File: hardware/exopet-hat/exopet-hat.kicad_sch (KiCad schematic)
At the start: 44 parts, among them J1 12V DC in, J10 CH3 12V OUT, J11 CH4 dry contact, J2 12V screw term, J3 RPi GPIO (HAT), J4 DS18B20 TRS jack, J5 DS18B20 JST, J8 CH1 12V OUT, J9 CH2 12V OUT, K1 G5LE-1 DC12, K2 G5LE-1 DC12, K3 G5LE-1 DC12, K4 G5LE-1 DC12, Q1 DMP4015SK3, U2 TBD62003APG, U4 CAT24C32, U5 TPD1E10B06

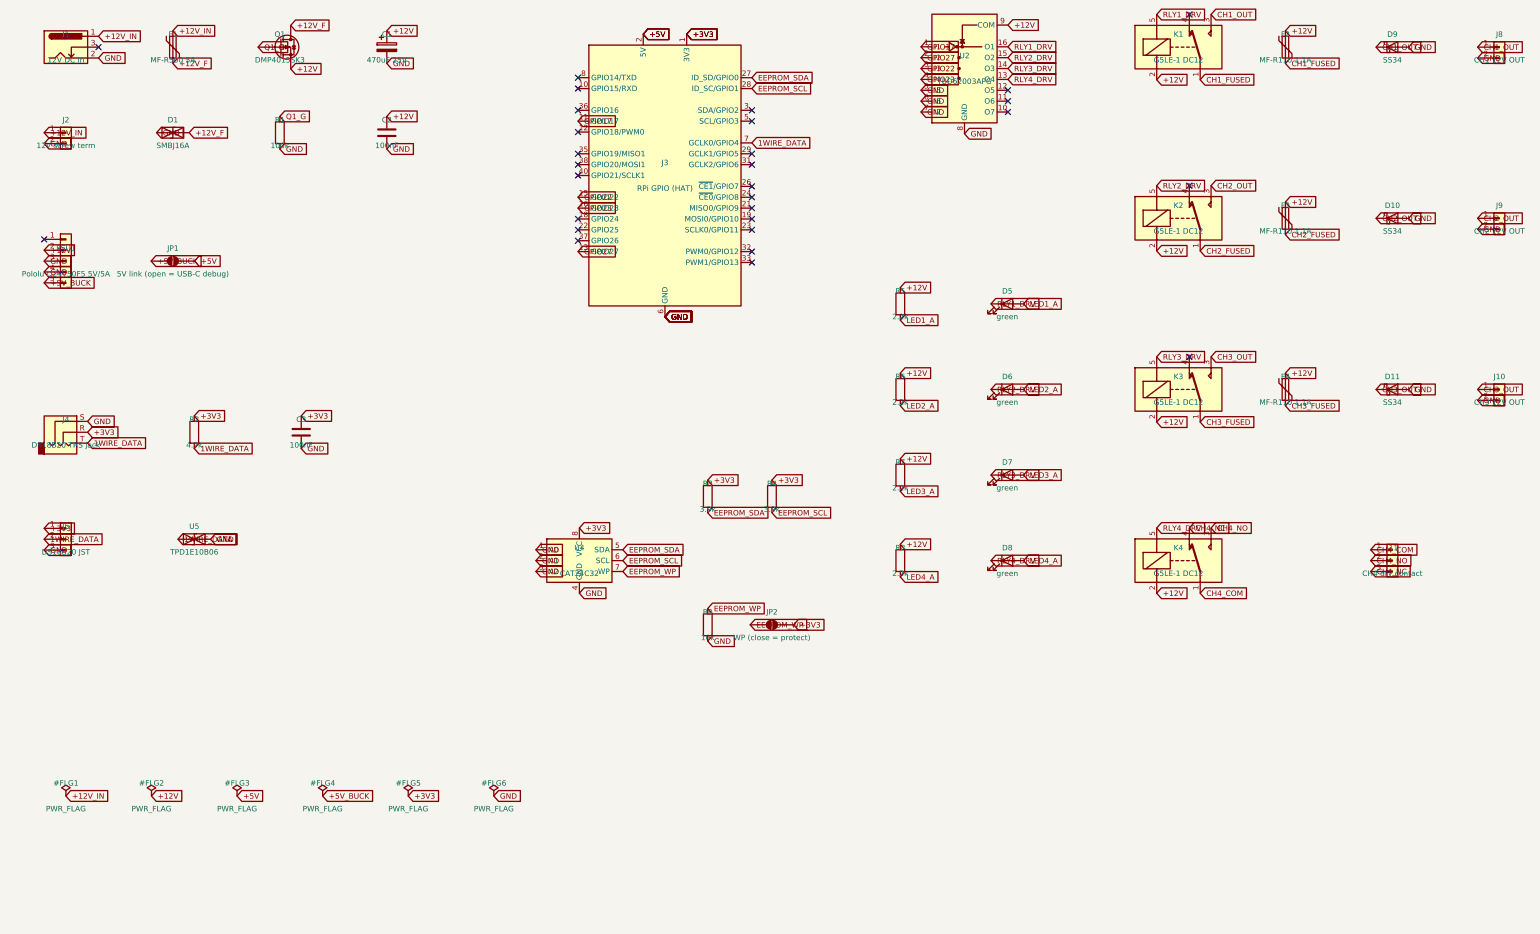
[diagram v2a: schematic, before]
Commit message: Assign footprints and LCSC part numbers to HAT schematic (stage 2)
- Every component has a footprint from the official KiCad libs (all
  verified to exist locally); BOM CSV exported grouped by value
- Web-verified LCSC picks: G5LE-1-CF relay C1524650, TBD62003AFG
  driver C163227 (SOIC), AOD403 P-FET C28969 (replaces unstocked
  DMP4015SK3)
- Added missing C4 EEPROM decoupling cap from spec
- BOM-NOTES.md records confidence per part and order-time checklist
- ERC still 0/0; netlist sanity re-verified

Co-Authored-By: Claude Fable 5 <noreply@anthropic.com>
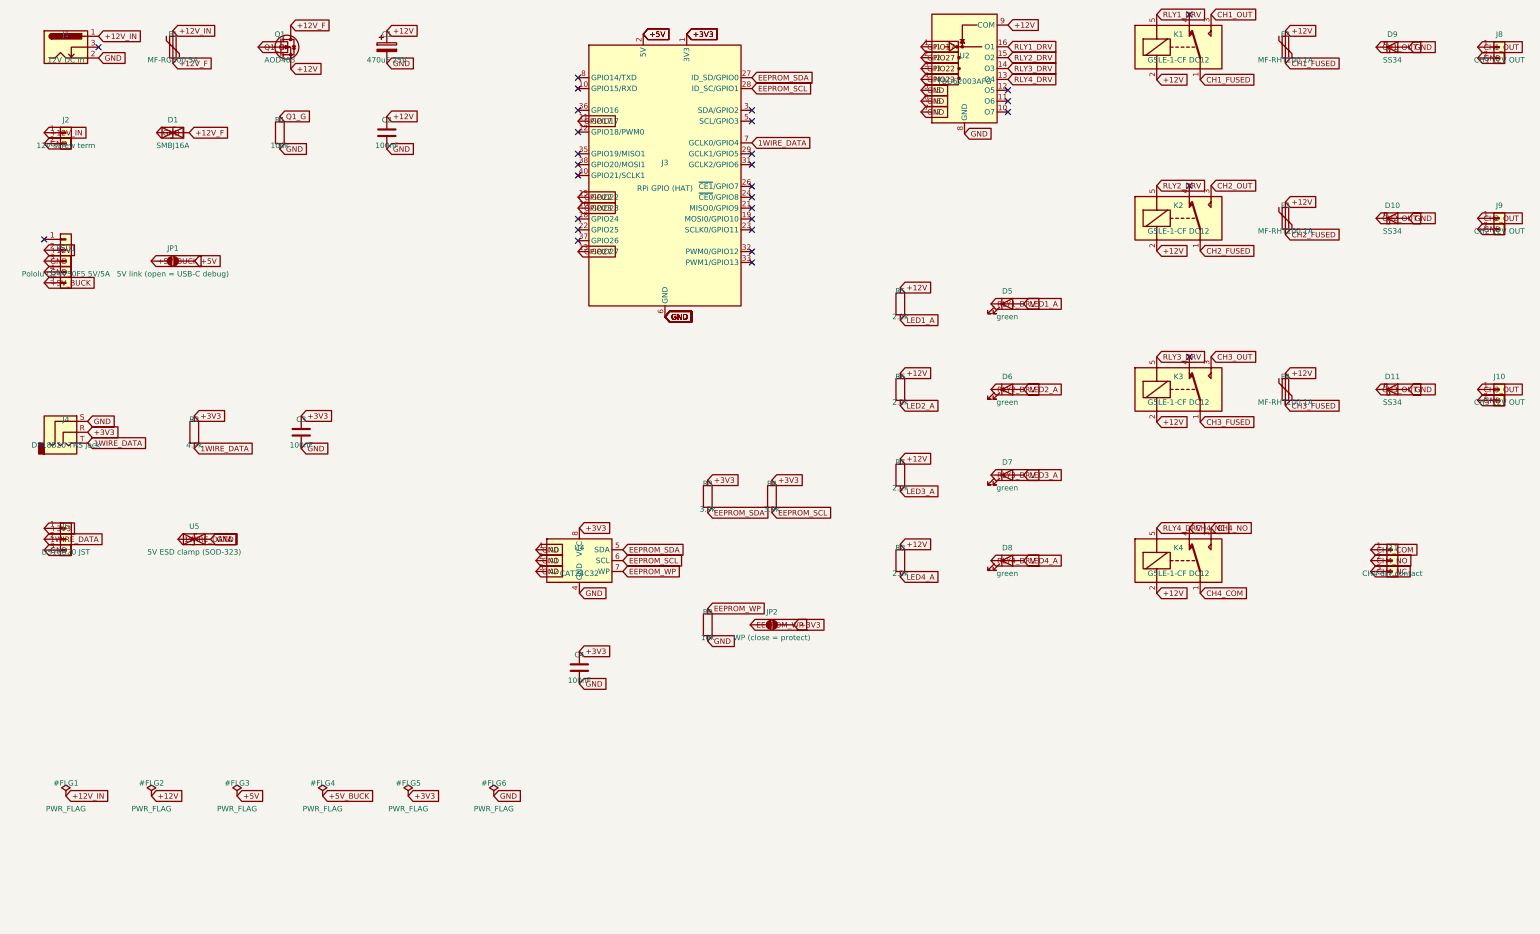
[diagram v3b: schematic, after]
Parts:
- added C4: 100nF, Capacitor_SMD:C_0805_2012Metric, symbol Device:C
- C1: footprint (none) -> Capacitor_THT:CP_Radial_D8.0mm_P3.50mm; LCSC (none) -> VERIFY
- C2, C3: footprint (none) -> Capacitor_SMD:C_0805_2012Metric; LCSC (none) -> C49678
- D1: footprint (none) -> Diode_SMD:D_SMB; LCSC (none) -> VERIFY
- D10, D11, D9: footprint (none) -> Diode_SMD:D_SMA; LCSC (none) -> C8678
- D5, D6, D7, D8: footprint (none) -> LED_SMD:LED_0805_2012Metric; LCSC (none) -> C2297
- F1: value MF-R500 5A -> MF-RG500 5A; footprint (none) -> Fuse:Fuse_Bourns_MF-RG500; LCSC (none) -> VERIFY
- F2, F3, F4: value MF-R110 1.1A -> MF-RHT100 1A; footprint (none) -> Fuse:Fuse_Bourns_MF-RHT100; LCSC (none) -> VERIFY
- J10, J2, J8, J9: footprint TerminalBlock:TerminalBlock_bornier-2_P5.08mm -> TerminalBlock_Phoenix:TerminalBlock_Phoenix_MKDS-1,5-2-5.08_1x02_P5.08mm_Horizontal
- J11: footprint TerminalBlock:TerminalBlock_bornier-3_P5.08mm -> TerminalBlock_Phoenix:TerminalBlock_Phoenix_MKDS-1,5-3-5.08_1x03_P5.08mm_Horizontal
- J3: footprint (none) -> Connector_PinSocket_2.54mm:PinSocket_2x20_P2.54mm_Vertical
- J4: footprint (none) -> Connector_Audio:Jack_3.5mm_CUI_SJ-3523-SMT_Horizontal
- J5: footprint (none) -> Connector_JST:JST_XH_B3B-XH-A_1x03_P2.50mm_Vertical
- JP1, JP2: footprint (none) -> Jumper:SolderJumper-2_P1.3mm_Open_RoundedPad1.0x1.5mm
- K1, K2, K3, K4: value G5LE-1 DC12 -> G5LE-1-CF DC12; LCSC (none) -> C1524650
- PSU1: footprint (none) -> Connector_PinSocket_2.54mm:PinSocket_1x05_P2.54mm_Vertical
- Q1: value DMP4015SK3 -> AOD403; footprint (none) -> Package_TO_SOT_SMD:TO-252-2; LCSC (none) -> C28969
- R1: footprint (none) -> Resistor_SMD:R_0805_2012Metric; LCSC (none) -> C17407
- R2: footprint (none) -> Resistor_SMD:R_0805_2012Metric; LCSC (none) -> C17673
- R3, R4: footprint (none) -> Resistor_SMD:R_0805_2012Metric; LCSC (none) -> C26010
- R5, R6, R7, R8: footprint (none) -> Resistor_SMD:R_0805_2012Metric; LCSC (none) -> C17520
- R9: footprint (none) -> Resistor_SMD:R_0805_2012Metric; LCSC (none) -> C17414
- U2: value TBD62003APG -> TBD62003AFG; footprint (none) -> Package_SO:SOIC-16_3.9x9.9mm_P1.27mm; LCSC (none) -> C163227
- U4: footprint (none) -> Package_SO:SOIC-8_3.9x4.9mm_P1.27mm; LCSC (none) -> VERIFY
- U5: value TPD1E10B06 -> 5V ESD clamp (SOD-323); footprint (none) -> Diode_SMD:D_SOD-323; LCSC (none) -> VERIFY
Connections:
- net +3V3: now also C4.1
- net GND: now also C4.2

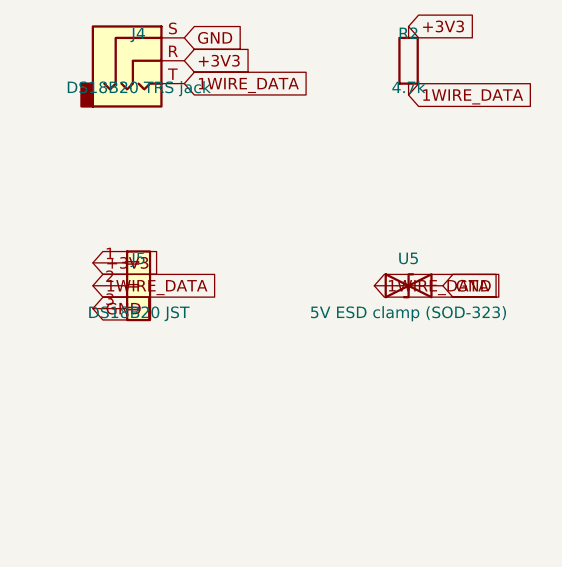
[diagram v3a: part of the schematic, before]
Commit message: Route ExoPet HAT board: generated placement + autoroute, DRC clean
- tools/gen_board.py builds the .kicad_pcb from the schematic netlist
  (footprints, per-pad nets, engineered placement, HAT outline/holes)
- All SMD on the back side in pin-free channels; top side THT only
- freerouting autoroutes (100 connections, 0 unrouted); GND pours both
  sides added and filled via pcbnew scripting
- DRC: 0 errors except 3 documented courtyard overlaps from
  flush-ganged terminal blocks
- Layout-driven design deltas: J5 JST temp connector cut (TRS only),
  J2 12V screw input became solder wire pads; schematic + BOM updated
- 3D renders of both sides included

Co-Authored-By: Claude Fable 5 <noreply@anthropic.com>
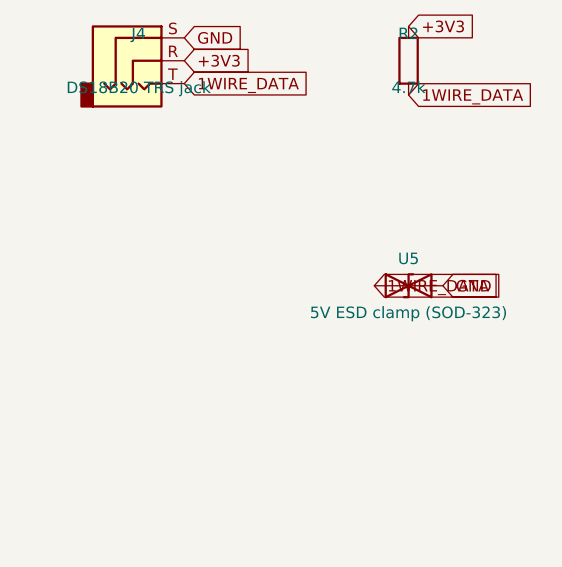
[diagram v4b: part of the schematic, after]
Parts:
- removed J5: DS18B20 JST, Connector_JST:JST_XH_B3B-XH-A_1x03_P2.50mm_Vertical, symbol Connector_Generic:Conn_01x03
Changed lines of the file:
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@@
-    )
-  )
-  (symbol (lib_id "Connector_Generic:Conn_01x03") (at 30 155 0) (unit 1)
-    (exclude_from_sim no) (in_bom yes) (on_board yes) (dnp no)
-    (property "Reference" "J5" (at 30 152 0) (effects (font (size 1.27 1.27))))
-    (property "Value" "DS18B20 JST" (at 30 158 0) (effects (font (size 1.27 1.27))))
-    (property "Footprint" "Connector_JST:JST_XH_B3B-XH-A_1x03_P2.50mm_Vertical" (at 30 155 0) (effects (font (size 1.27 1.27)) hide))
-    (property "LCSC" "" (at 30 155 0) (effects (font (size 1.27 1.27)) hide))
-    (pin "1")
-    (pin "2")
-    (pin "3")
-    (instances
-      (project "exopet-hat"
-        (path "/e0a7e100-0000-4000-8000-00000000c0de" (reference "J5") (unit 1))
-      )
     )
   )
@@
   (global_label "+3V3" (shape input) (at 35.08 130.0 0) (effects (font (size 1.27 1.27)) (justify left)))
   (global_label "1WIRE_DATA" (shape input) (at 35.08 132.54 0) (effects (font (size 1.27 1.27)) (justify left)))
-  (global_label "+3V3" (shape input) (at 24.92 152.46 0) (effects (font (size 1.27 1.27)) (justify left)))
-  (global_label "1WIRE_DATA" (shape input) (at 24.92 155.0 0) (effects (font (size 1.27 1.27)) (justify left)))
-  (global_label "GND" (shape input) (at 24.92 157.54 0) (effects (font (size 1.27 1.27)) (justify left)))
   (global_label "+3V3" (shape input) (at 60.0 126.19 0) (effects (font (size 1.27 1.27)) (justify left)))
   (global_label "1WIRE_DATA" (shape input) (at 60.0 133.81 0) (effects (font (size 1.27 1.27)) (justify left)))

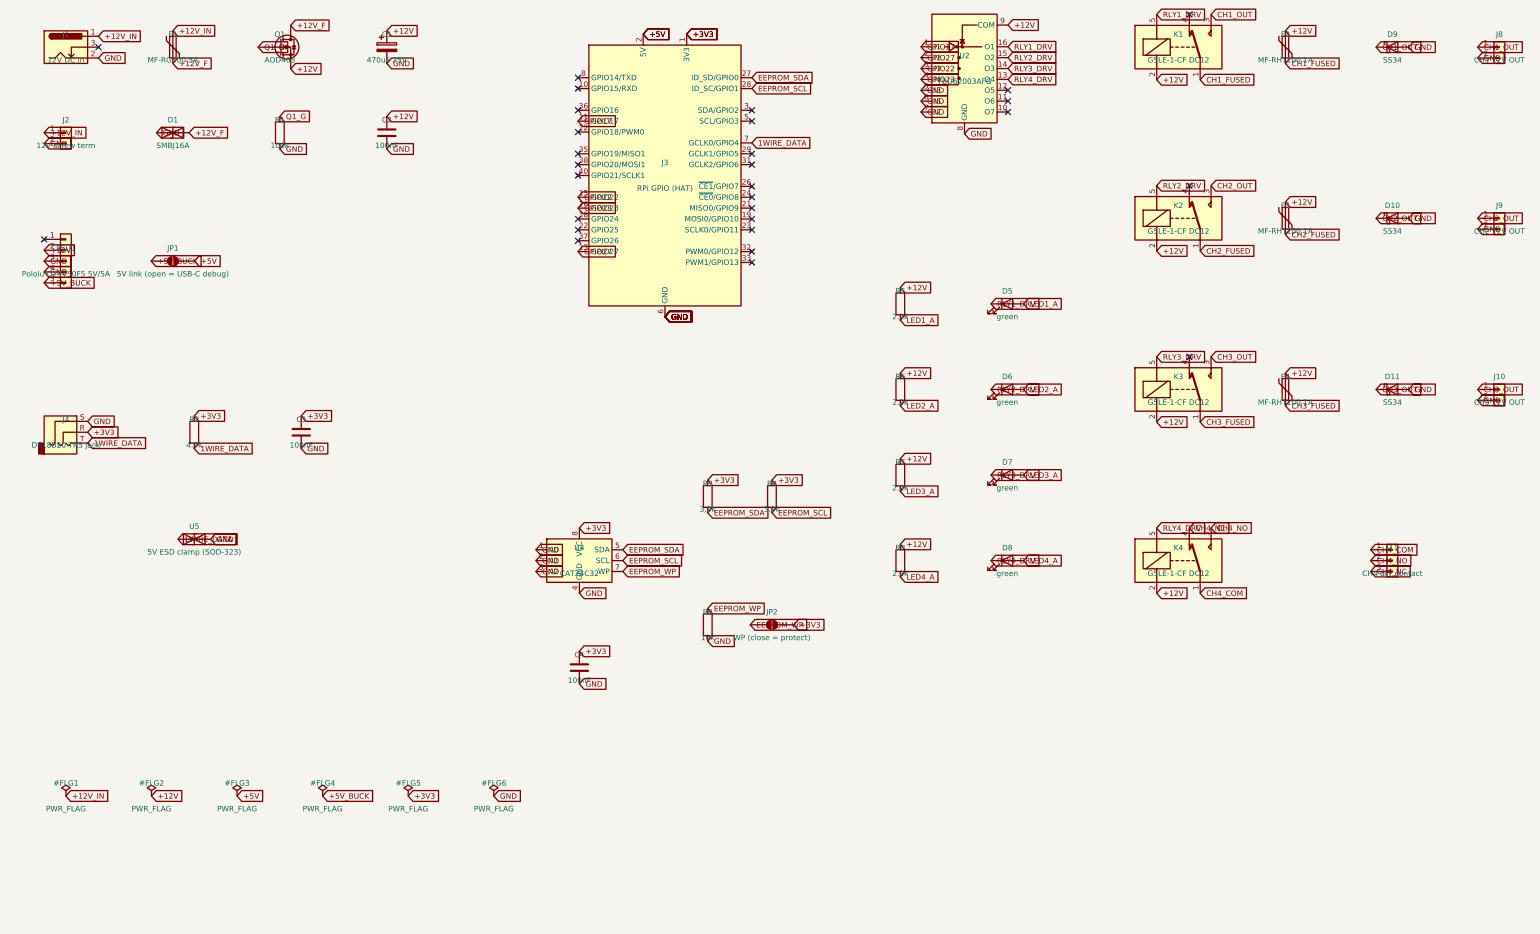
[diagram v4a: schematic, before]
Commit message: Regroup HAT terminals per function; add float switch inputs
- Front edge: CH1/CH2/CH3 switched-12V blocks separated, CH4 dry
  contact last; left edge: FLOAT1, FLOAT2, TEMP sensor stack
- Temperature input is now a 3-pos screw terminal (TRS jack and JST
  both removed) - bare probe wires screw straight in
- Added the missing float switch inputs: GPIO16 (tank, matches hub
  code) and GPIO12 (sump spec), each with 10k pull-up, 1k series
  resistor, and 100nF filter
- All terminals now Phoenix PT-1,5 3.5mm; J2 aux 12V input removed
  (barrel jack sole input)
- Rerouted: 112 connections, 0 unrouted; DRC fully clean (0 violations)

Co-Authored-By: Claude Fable 5 <noreply@anthropic.com>
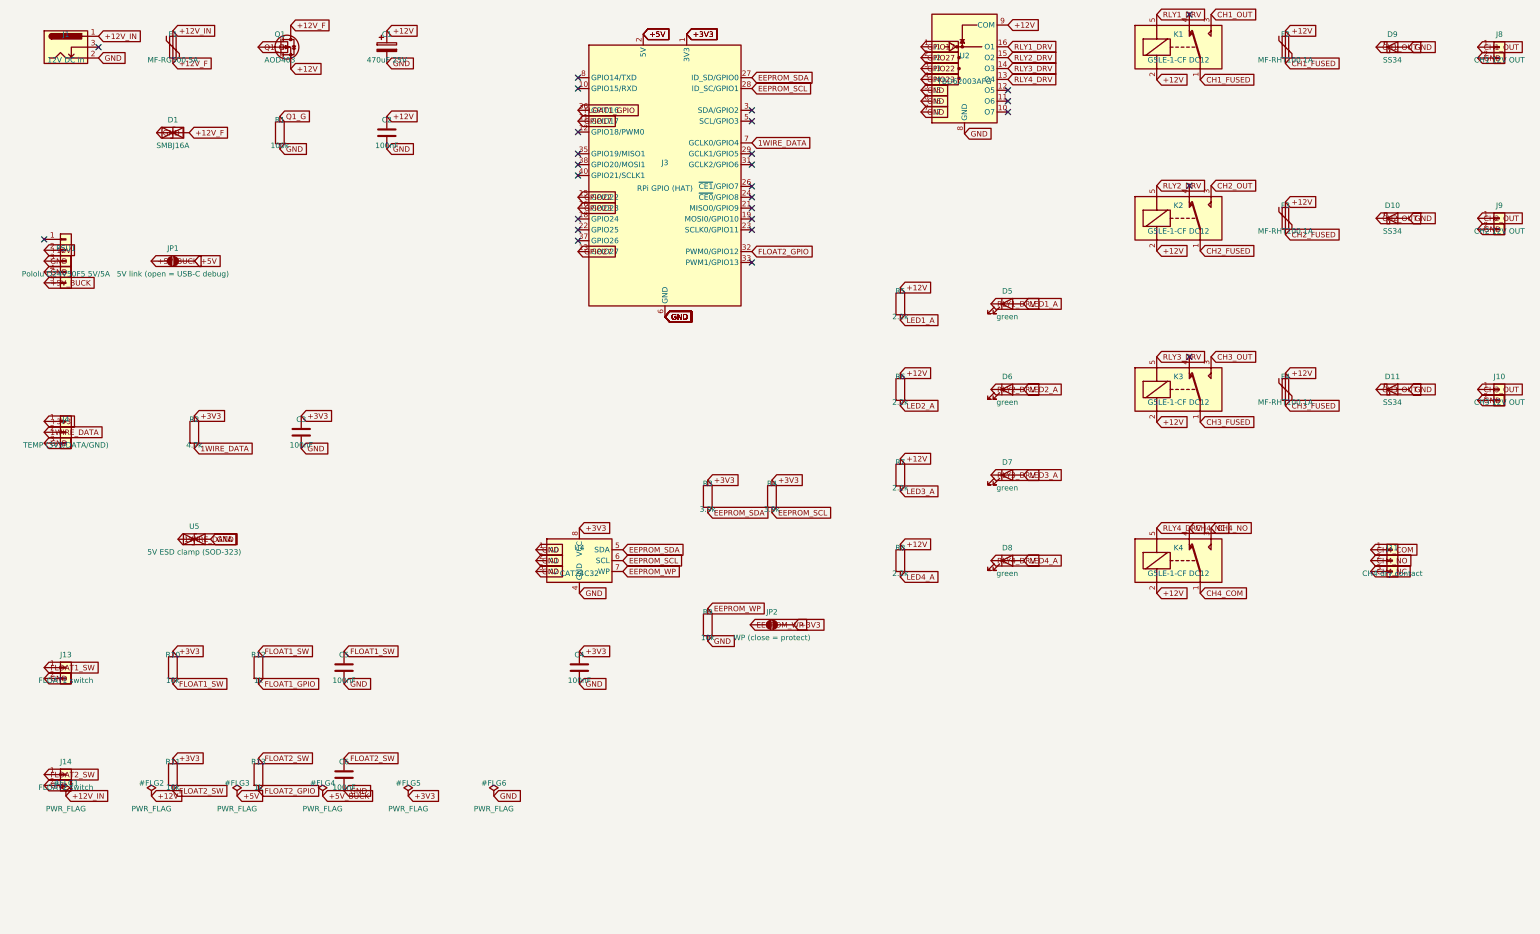
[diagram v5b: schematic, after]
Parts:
- removed J2: 12V screw term, TerminalBlock_Phoenix:TerminalBlock_Phoenix_MKDS-1,5-2-5.08_1x02_P5.08mm_Horizontal, symbol Connector_Generic:Conn_01x02
- added C5, C6: 100nF, Capacitor_SMD:C_0805_2012Metric, symbol Device:C
- added J13: FLOAT1 switch, TerminalBlock_Phoenix:TerminalBlock_Phoenix_PT-1,5-2-3.5-H_1x02_P3.50mm_Horizontal, symbol Connector_Generic:Conn_01x02
- added J14: FLOAT2 switch, TerminalBlock_Phoenix:TerminalBlock_Phoenix_PT-1,5-2-3.5-H_1x02_P3.50mm_Horizontal, symbol Connector_Generic:Conn_01x02
- added R10, R11: 10k, Resistor_SMD:R_0805_2012Metric, symbol Device:R
- added R12, R13: 1k, Resistor_SMD:R_0805_2012Metric, symbol Device:R
- J10, J8, J9: footprint TerminalBlock_Phoenix:TerminalBlock_Phoenix_MKDS-1,5-2-5.08_1x02_P5.08mm_Horizontal -> TerminalBlock_Phoenix:TerminalBlock_Phoenix_PT-1,5-2-3.5-H_1x02_P3.50mm_Horizontal
- J11: footprint TerminalBlock_Phoenix:TerminalBlock_Phoenix_MKDS-1,5-3-5.08_1x03_P5.08mm_Horizontal -> TerminalBlock_Phoenix:TerminalBlock_Phoenix_PT-1,5-3-3.5-H_1x03_P3.50mm_Horizontal
- J4: value DS18B20 TRS jack -> TEMP (3V3/DATA/GND); footprint Connector_Audio:Jack_3.5mm_CUI_SJ-3523-SMT_Horizontal -> TerminalBlock_Phoenix:TerminalBlock_Phoenix_PT-1,5-3-3.5-H_1x03_P3.50mm_Horizontal; symbol Connector_Audio:AudioJack3 -> Connector_Generic:Conn_01x03
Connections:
- net +3V3: now also J4.1 (Pin_1), R10.1, R11.1; no longer J4.R
- net 1WIRE_DATA: now also J4.2 (Pin_2); no longer J4.T
- net GND: now also J4.3 (Pin_3), C5.2, C6.2, J13.2 (Pin_2), J14.2 (Pin_2); no longer J4.S
- net FLOAT2_GPIO: now reaches J3.32 (PWM0/GPIO12)
- net FLOAT2_GPIO: now also R13.2
- net FLOAT1_GPIO: now reaches J3.36 (GPIO16)
- net FLOAT1_GPIO: now also R12.2
- new net FLOAT1_SW: C5.1, J13.1 (Pin_1), R10.2, R12.1
- new net FLOAT2_SW: C6.1, J14.1 (Pin_1), R11.2, R13.1
- no-connect marks 29 -> 27
